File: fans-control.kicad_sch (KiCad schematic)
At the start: 36 parts

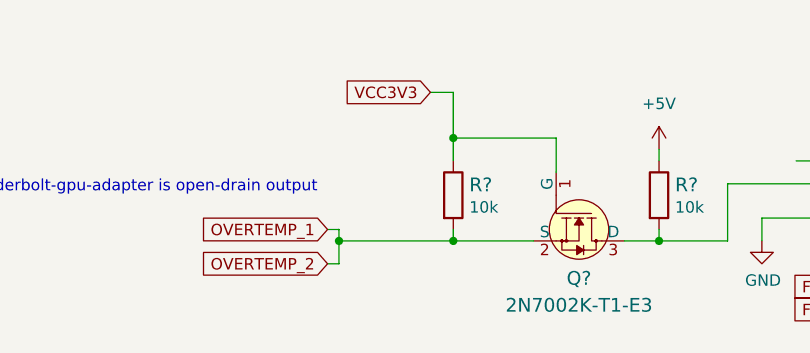
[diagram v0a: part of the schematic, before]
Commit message: Change power flags on schematic
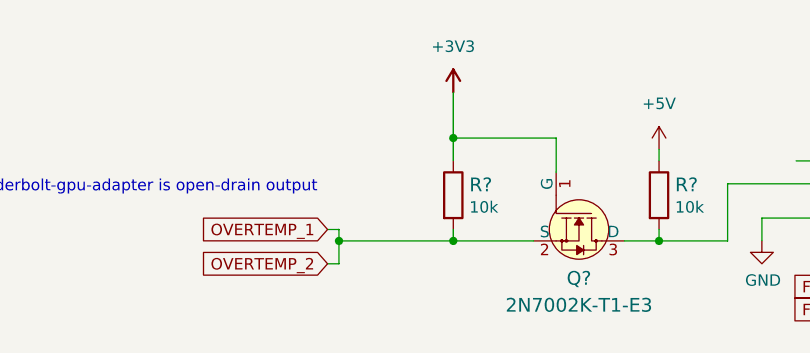
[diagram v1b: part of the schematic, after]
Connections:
- net VCC3V3 renamed +3V3
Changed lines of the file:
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@@
     (stroke (width 0) (type default) (color 0 0 0 0))
   )
-  (wire (pts (xy 173.99 53.34) (xy 176.53 53.34))
-    (stroke (width 0) (type default) (color 0 0 0 0))
-  )
   (wire (pts (xy 80.01 198.12) (xy 55.88 198.12))
     (stroke (width 0) (type default) (color 0 0 0 0))
@@
     )
   )
-  (global_label "VCC3V3" (shape input) (at 173.99 53.34 180) (fields_autoplaced)
-    (effects (font (size 1.27 1.27)) (justify right))
-    (property "Intersheet References" "${INTERSHEET_REFS}" (id 0) (at 43.18 -100.33 0)
-      (effects (font (size 1.27 1.27)) hide)
-    )
-  )
   (global_label "VCC12V0" (shape input) (at 384.81 77.47 0) (fields_autoplaced)
     (effects (font (size 1.27 1.27)) (justify left))
@@
     )
     (pin "1")
+  )
+  (symbol (lib_id "antmicropower:+3V3") (at 176.53 53.34 0) (unit 1)
+    (in_bom yes) (on_board yes) (fields_autoplaced)
+    (property "Reference" "#PWR?" (id 0) (at 191.77 55.88 0)
+      (effects (font (size 1.27 1.27) (thickness 0.15)) (justify left bottom) hide)
+    )
+    (property "Value" "+3V3" (id 1) (at 176.53 48.26 0)
+      (effects (font (size 1.27 1.27) (thickness 0.15)))
+    )
+    (property "Footprint" "" (id 2) (at 191.77 60.96 0)
+      (effects (font (size 1.27 1.27) (thickness 0.15)) (justify left bottom) hide)
+    )
+    (property "Datasheet" "" (id 3) (at 191.77 63.5 0)
+      (effects (font (size 1.27 1.27) (thickness 0.15)) (justify left bottom) hide)
+    )
+    (property "Author" "Antmicro" (id 4) (at 191.77 60.96 0)
+      (effects (font (size 1.27 1.27) (thickness 0.15)) (justify left bottom) hide)
+    )
+    (property "License" "Apache-2.0" (id 5) (at 191.77 63.5 0)
+      (effects (font (size 1.27 1.27) (thickness 0.15)) (justify left bottom) hide)
+    )
+    (pin "1")

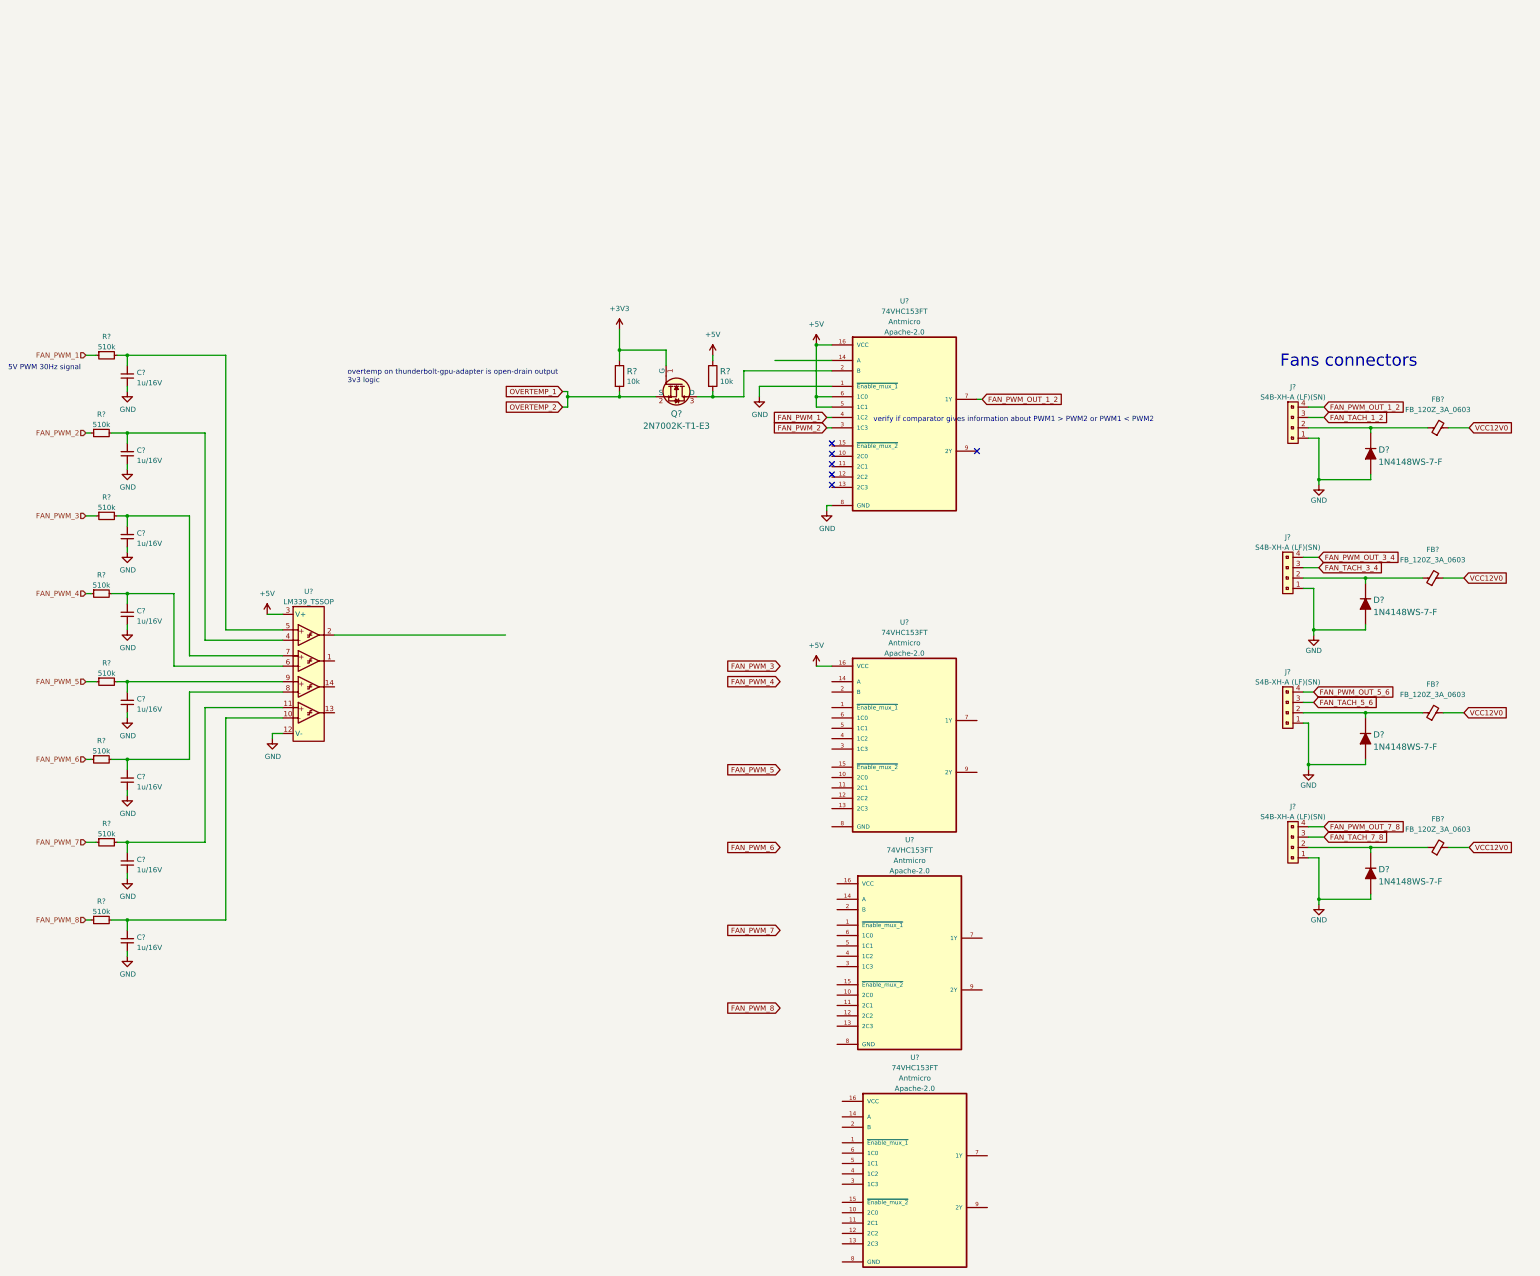
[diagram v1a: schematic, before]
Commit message: Reannotate schematic symbols
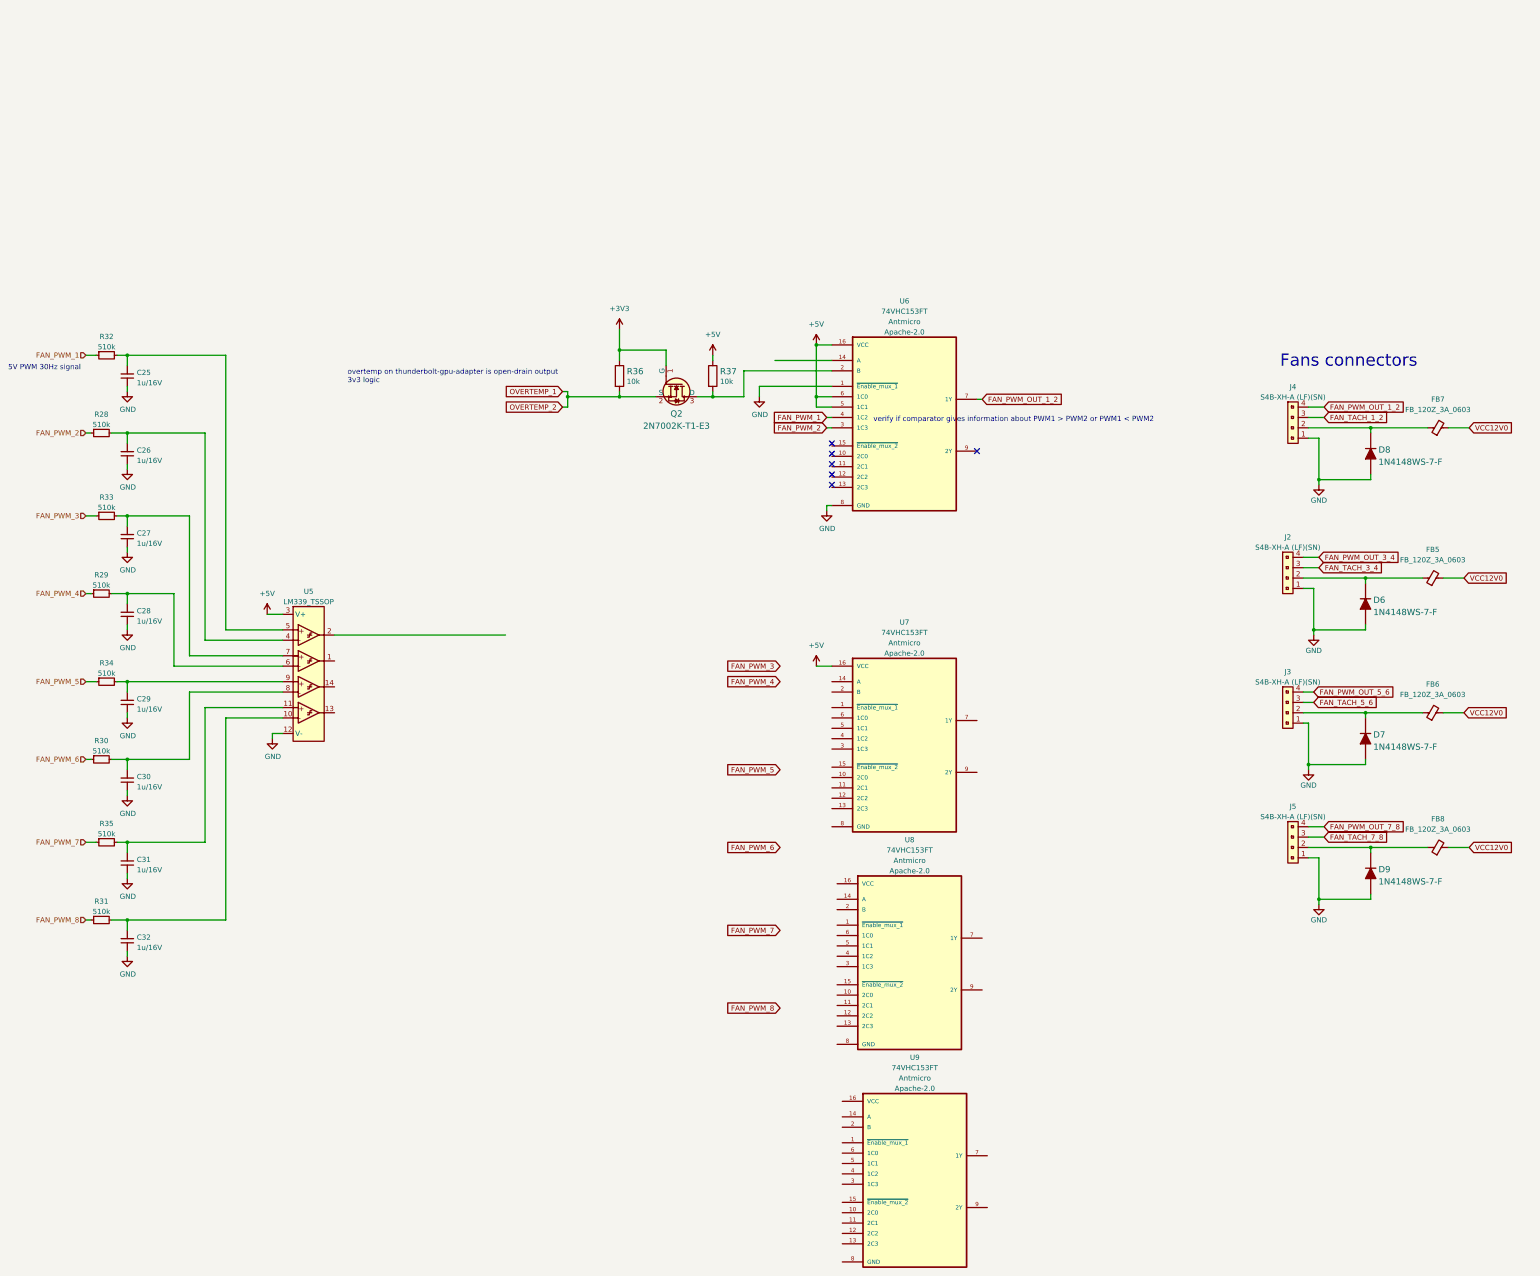
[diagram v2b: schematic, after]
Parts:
- gave numbers to parts that had none: 36

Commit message: Add filtration for fan arbiters
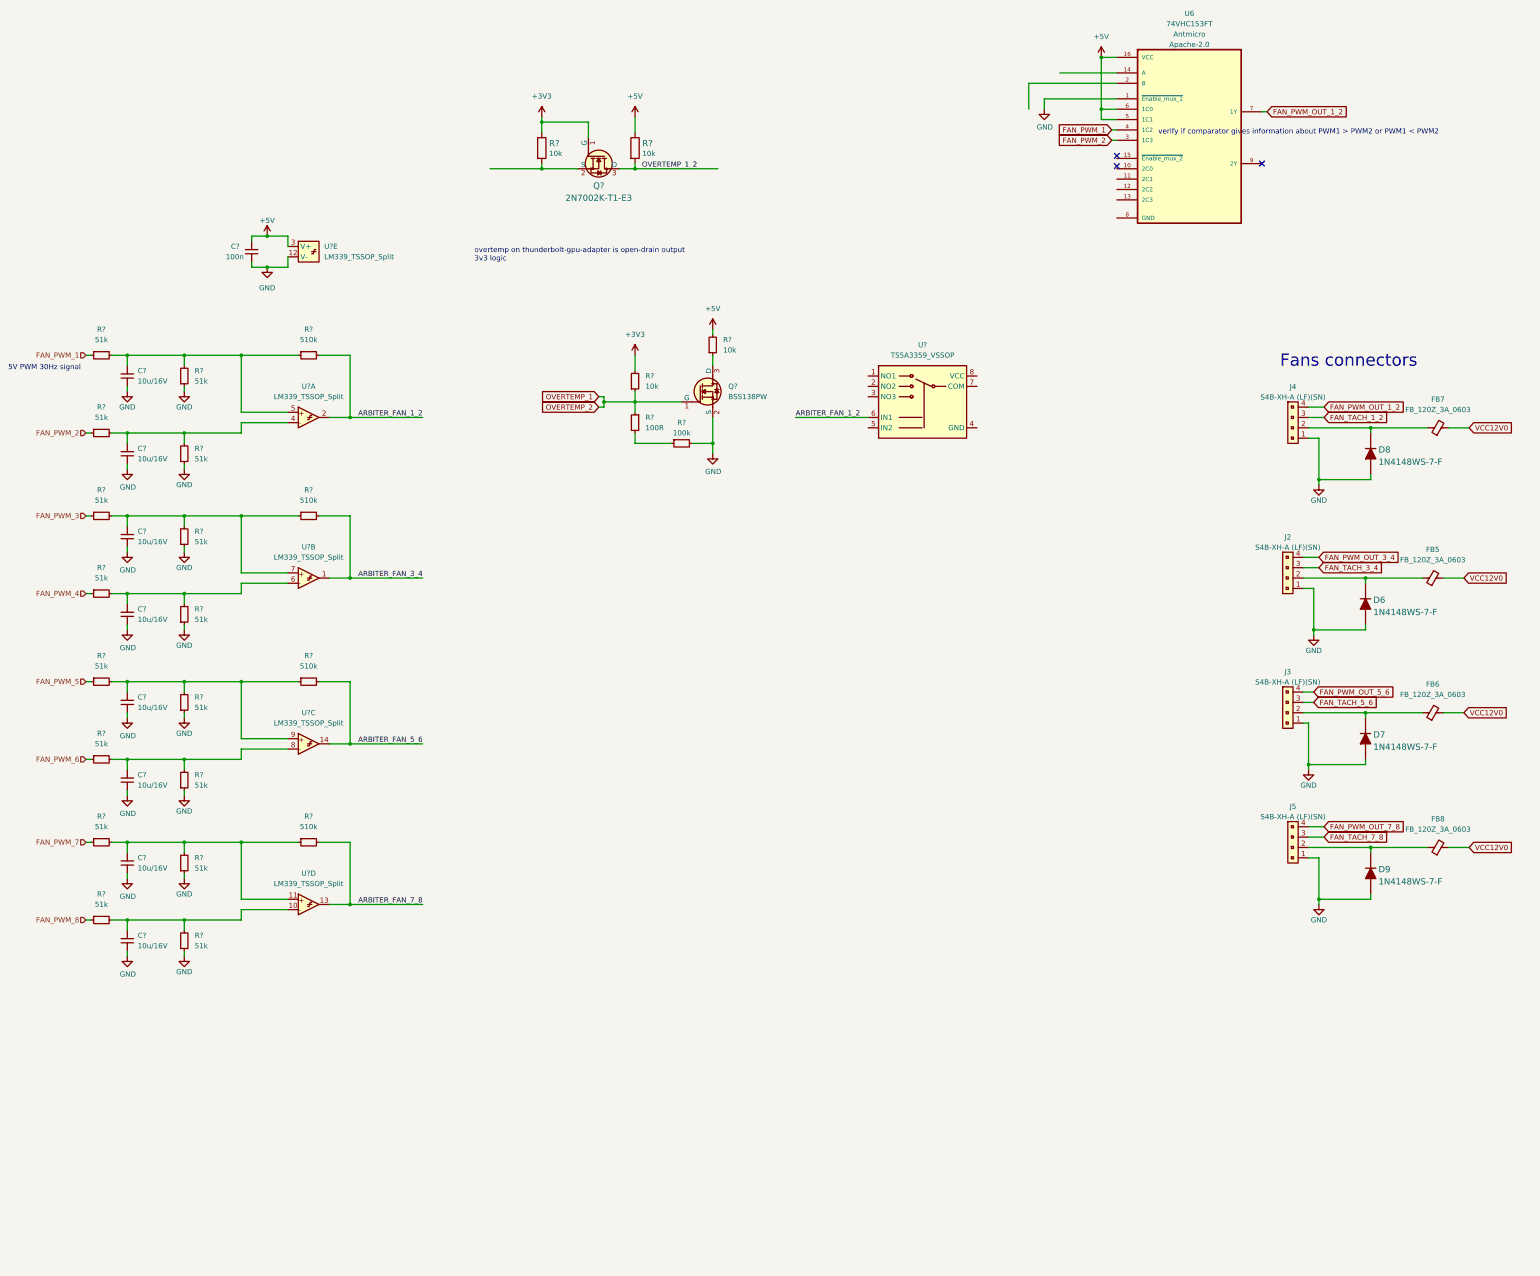
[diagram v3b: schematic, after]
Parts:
- removed C25, C26, C27, C28, C29, C30, C31, C32: C_1u_16V_0402, antmicro-footprints:C_0402_1005Metric, symbol antmicroCapacitors0402:C_1u_16V_0402
- removed Q2: 2N7002K-T1-E3, antmicro-footprints:SOT-23-3, symbol antmicroTransistorsFETsMOSFETsSingle:2N7002K-T1-E3
- removed R28, R29, R30, R31, R32, R33, R34, R35: R_510k_0402, antmicro-footprints:R_0402_1005Metric, symbol antmicroResistors0402:R_510k_0402
- removed R36, R37: R_10k_0402, antmicro-footprints:R_0402_1005Metric, symbol antmicroResistors0402:R_10k_0402
- removed U5: LM339_TSSOP, antmicro-footprints:TSSOP-14_4.4x5mm_P0.65mm, symbol antmicroOperationalAmplifiers:LM339_TSSOP
- removed U7, U8, U9: 74VHC153FT, antmicro-footprints:TSSOP-16_4.4x5mm_P0.65mm, symbol antmicroInterfaceAnalogSwitchesMultiplexersDemultiplexers:74VHC153FT
- added C? (x8): C_10u_16V_0603, antmicro-footprints:C_0603_1608Metric, symbol antmicroCapacitors0603:C_10u_16V_0603
- added C?: C_100n_0402, antmicro-footprints:C_0402_1005Metric, symbol antmicroCapacitors0402:C_100n_0402
- added Q?: 2N7002K-T1-E3, antmicro-footprints:SOT-23-3, symbol antmicroTransistorsFETsMOSFETsSingle:2N7002K-T1-E3
- added Q?: BSS138PW, antmicro-footprints:SC70-3, symbol antmicroTransistorsFETsMOSFETsSingle:BSS138PW
- added R? (x16): R_51k_0402, antmicro-footprints:R_0402_1005Metric, symbol antmicroResistors0402:R_51k_0402
- added R? (x4): R_10k_0402, antmicro-footprints:R_0402_1005Metric, symbol antmicroResistors0402:R_10k_0402
- added R? (x4): R_510k_0402, antmicro-footprints:R_0402_1005Metric, symbol antmicroResistors0402:R_510k_0402
- added R?: R_100k_0402, antmicro-footprints:R_0402_1005Metric, symbol antmicroResistors0402:R_100k_0402
- added R?: R_100R_0402, antmicro-footprints:R_0402_1005Metric, symbol antmicroResistors0402:R_100R_0402
- added U? (x5): LM339_TSSOP_Split, antmicro-footprints:TSSOP-14_4.4x5mm_P0.65mm, symbol antmicroOperationalAmplifiers:LM339_TSSOP_Split
- added U?: TS5A3359_VSSOP, antmicro-footprints:VSSOP-8_2.3x2mm_P0.5mm, symbol antmicroInterfaceAnalogSwitchesMultiplexersDemultiplexers:TS5A3359_VSSOP
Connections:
- net +3V3: now also Q?.1 (G), R?.1, R?.2
- net +5V: now also C?.2, R?.1, R?.2, U?.3 (V+)
- net FAN_PWM_1: now also R?.1
- net FAN_PWM_2: now also R?.1
- net FAN_PWM_3: now also R?.1
- net FAN_PWM_4: now also R?.1
- net FAN_PWM_5: now also R?.1
- net FAN_PWM_6: now also R?.1
- net FAN_PWM_7: now also R?.1
- net FAN_PWM_8: now also R?.1
- net GND: now also C?.1, C?.1, C?.1, C?.1, C?.1, C?.1, C?.1, C?.1, C?.1, Q?.2 (S), R?.1, R?.1, R?.1, R?.1, R?.1, R?.1, R?.1, R?.1, R?.2, U?.12 (V-); no longer U6.8 (GND)
- net OVERTEMP_1: now also Q?.1 (G), R?.1, R?.1
- new net: C?.2, R?.2, R?.2, U?.6
- new net: C?.2, R?.2, R?.2, U?.4
- new net: Q?.2 (S), R?.2
- new net: C?.2, R?.2, R?.2, U?.10
- new net: C?.2, R?.1, R?.2, R?.2, U?.7
- new net: C?.2, R?.1, R?.2, R?.2, U?.11
- new net: Q?.3 (D), R?.1
- new net: C?.2, R?.1, R?.2, R?.2, U?.5
- new net: C?.2, R?.1, R?.2, R?.2, U?.9
- new net: R?.1, R?.2
- new net: C?.2, R?.2, R?.2, U?.8
- new net ARBITER_FAN_1_2: R?.2, U?.2, U?.6 (IN1)
- new net ARBITER_FAN_3_4: R?.2, U?.1
- new net ARBITER_FAN_5_6: R?.2, U?.14
- new net ARBITER_FAN_7_8: R?.2, U?.13
- new net OVERTEMP_1_2: Q?.3 (D), R?.2
- no-connect marks 6 -> 3
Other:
- moved on the sheet: U6

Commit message: Repleace non standard components in connectors and ftdi and power
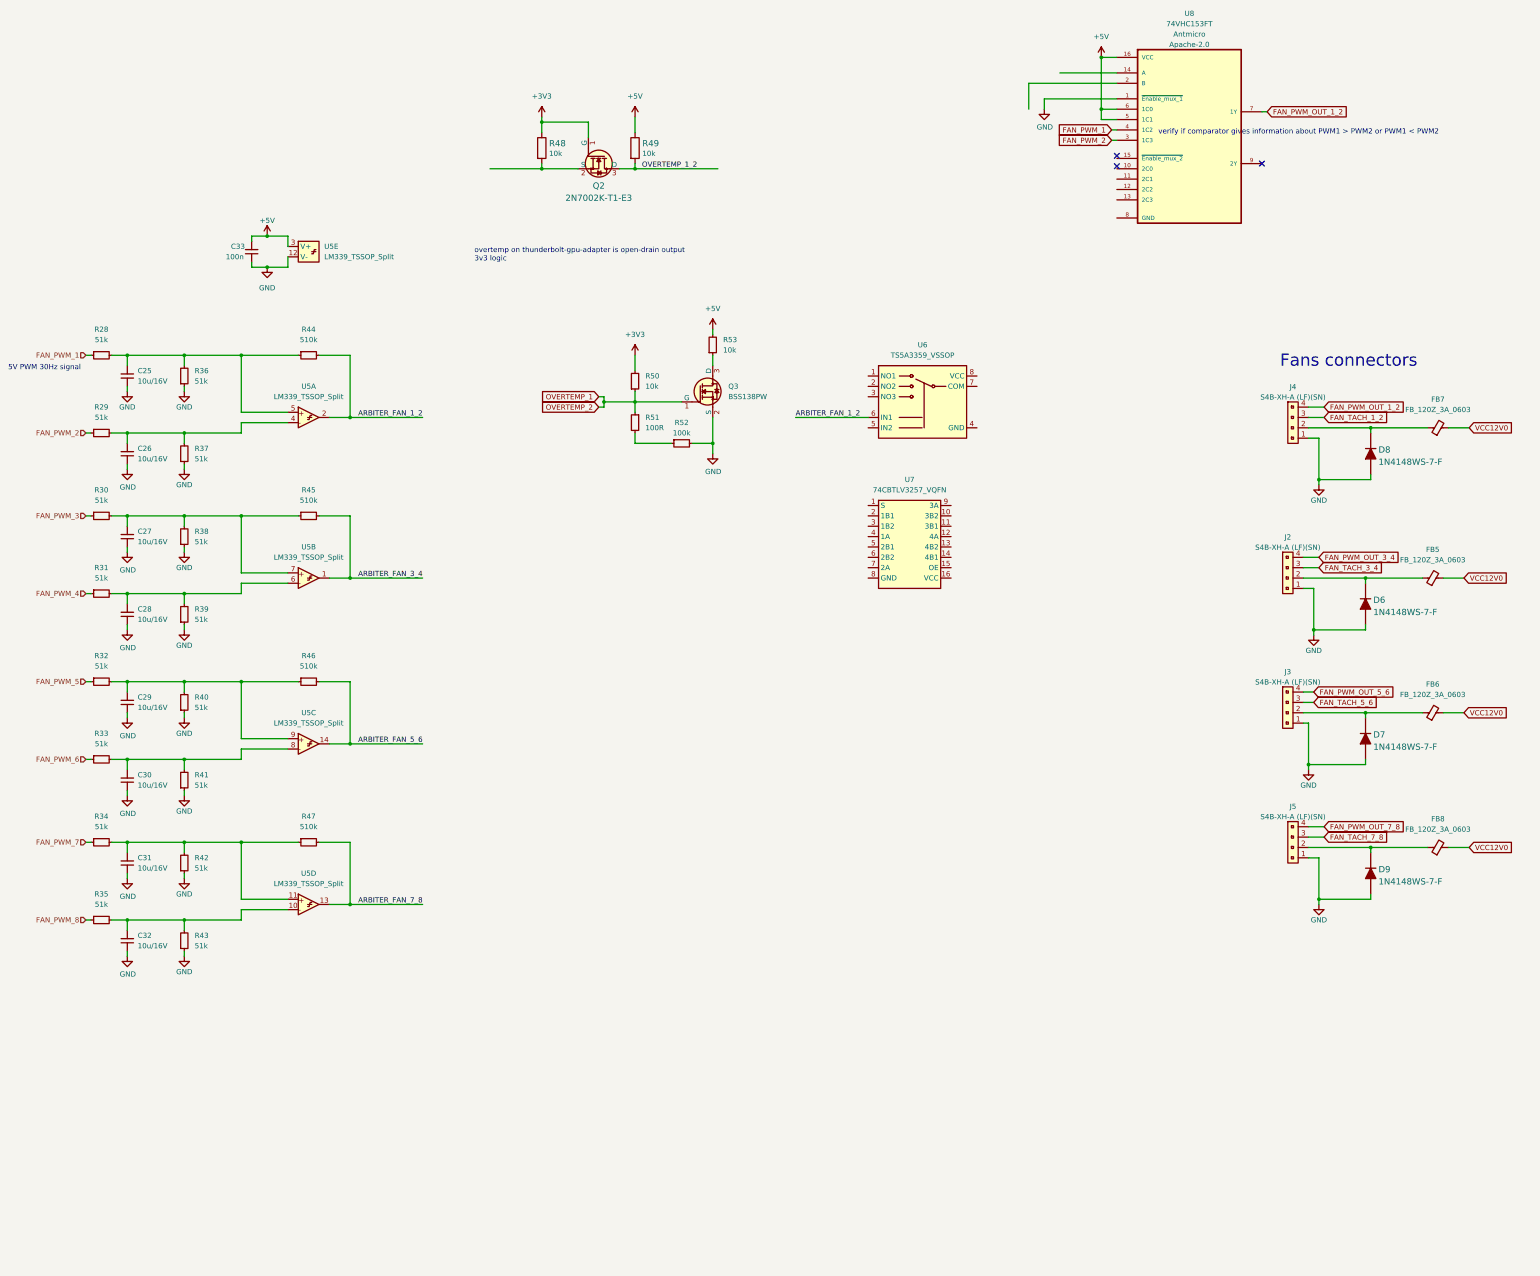
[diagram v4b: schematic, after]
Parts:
- added U7: 74CBTLV3257_VQFN, antmicro-footprints:DHVQFN-16-1EP_2.5x3.5mm_P0.5mm, symbol antmicroInterfaceAnalogSwitchesMultiplexersDemultiplexers:74CBTLV3257_VQFN
- gave numbers to parts that had none: 39
- renumbered U6 to U8
